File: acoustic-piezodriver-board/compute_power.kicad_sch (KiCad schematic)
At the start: 26 parts, among them J301 Conn_02x06_Odd_Even, U10 NCE6005AS, U9 LM3478MM

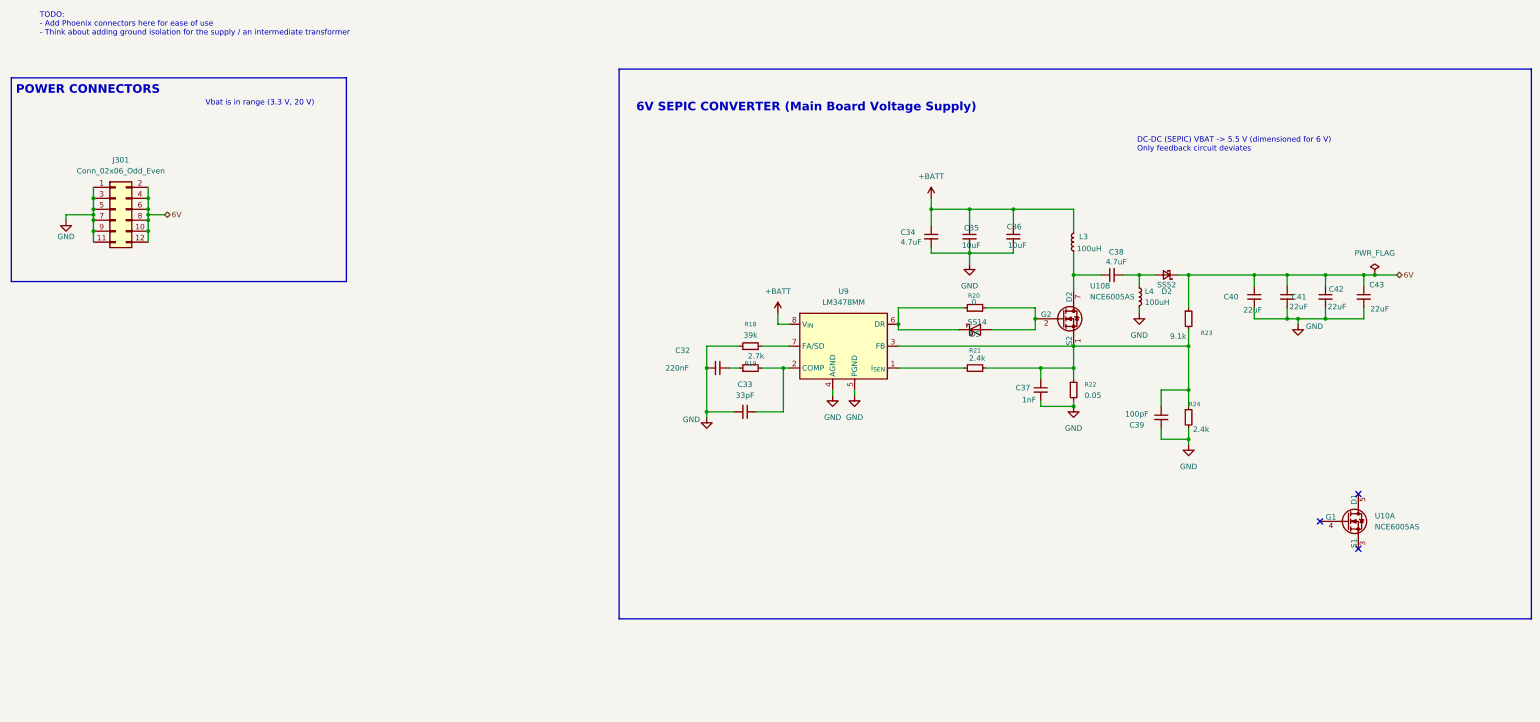
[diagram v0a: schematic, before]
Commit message: [schematic] added adc for temperature measurement, current sense resistors, [layout] component placement, connector placement
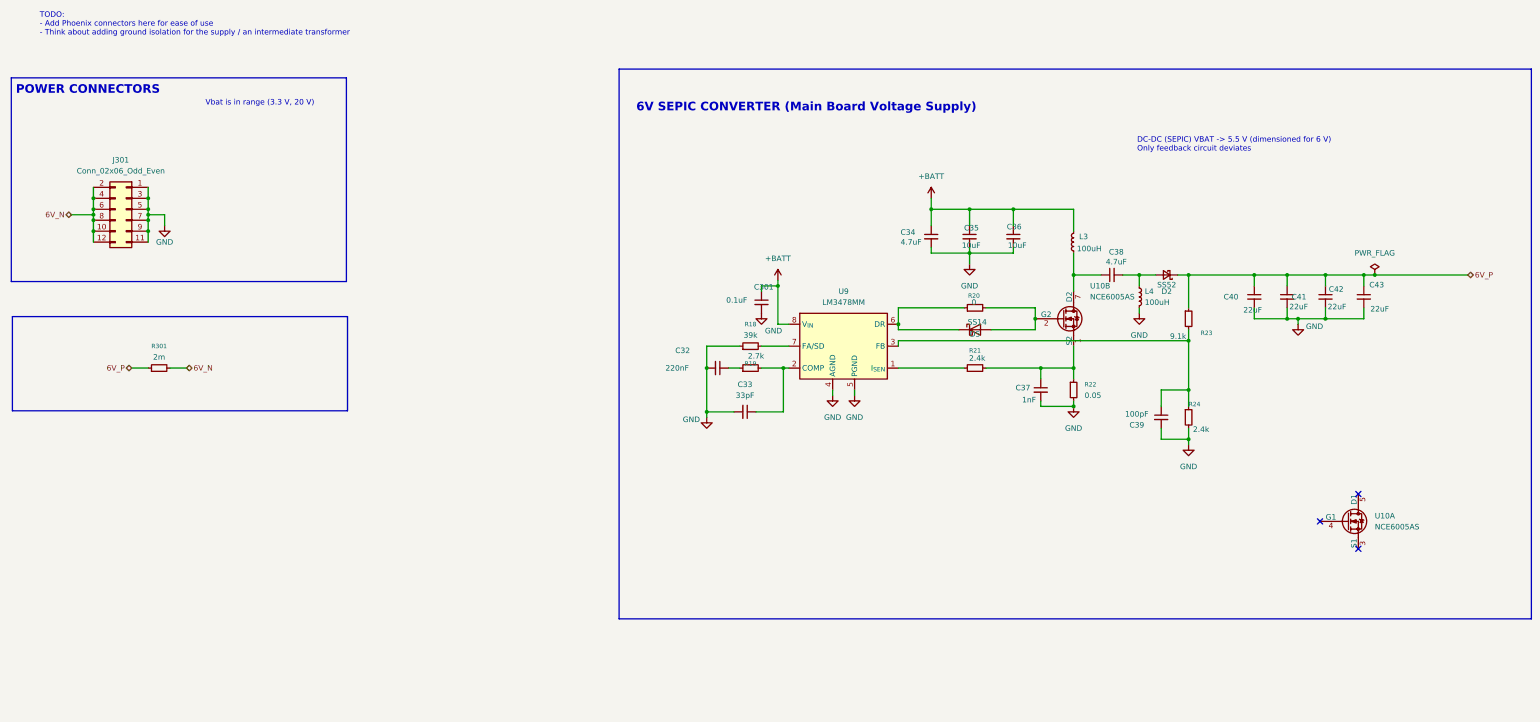
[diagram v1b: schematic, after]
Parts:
- added C301: 0.1uF, Capacitor_SMD:C_0201_0603Metric, symbol Device:C_Small
- added R301: 2m, Resistor_SMD:R_2512_6332Metric, symbol Device:R_Small
- J301: footprint Connector_PinHeader_2.54mm:PinHeader_2x06_P2.54mm_Horizontal -> Connector_PinHeader_2.54mm:PinHeader_2x06_P2.54mm_Vertical; LPN (none) -> C124388; MPN (none) -> B-2100S12P-B110
- L4: footprint (none) -> iw-inductor:PSPMAC1045H-101M-ANP
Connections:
- net +BATT: now also C301.1
- net GND: now also C301.2
- net at C39.1, R23.2, R24.1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: no longer C37.1, R21.2, R22.1, U10.1 (S2)
- net 6V renamed 6V_N
- net 6V_N: now also R301.2; no longer C40.1, C41.1, C42.1, C43.1, D2.1 (K), R23.1
- new net: C37.1, R21.2, R22.1, U10.1 (S2)
- new net 6V_P: C40.1, C41.1, C42.1, C43.1, D2.1 (K), R23.1, R301.1

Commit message: found hal-sensor, replaced with different one for lower voltage signal source impedance, reorganised schematic
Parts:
- added C302: 0.1uF, Capacitor_SMD:C_0402_1005Metric, symbol Device:C_Small
- added C303: 1nF, Capacitor_SMD:C_0402_1005Metric, symbol Device:C_Small
- added TP301: TestPoint_Probe, TestPoint:TestPoint_Pad_D1.0mm, symbol Connector:TestPoint_Probe
- added U301: ACS711xEXLT-15AB, Sensor_Current:Allegro_QFN-12-10-1EP_3x3mm_P0.5mm, symbol Sensor_Current:ACS711xEXLT-15AB
- R301: value 2m -> 1k; footprint Resistor_SMD:R_2512_6332Metric -> Resistor_SMD:R_0603_1608Metric; LPN C160590 -> C21190; MPN RLP25FEER002 -> 0603WAF1001T5E
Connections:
- net 6V_N: now also U301.2 (IP-); no longer R301.2
- net 6V_P: now also U301.1 (IP+); no longer R301.1
- net GND: now also C302.2, C303.2, U301.3 (GND), U301.5 (NC), U301.6 (NC), U301.7 (NC), U301.8 (NC)
- new net: R301.2, TP301.1, U301.4 (~{FAULT})
- new net +3V3: C302.1, R301.1, U301.10 (VCC)
- new net ADC_IFPGA: C303.1, U301.9 (VIOUT)
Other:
- note added: "- Differential -> Single-ended input - Buffering - Amplification (range 0.1 -> 2 Amps), increments of 0.01"
- note added: "I_FPGA measurement"

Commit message: added new notes + schematic component hal sensors
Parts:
- removed C302: 0.1uF, Capacitor_SMD:C_0402_1005Metric, symbol Device:C_Small
- removed C303: 1nF, Capacitor_SMD:C_0402_1005Metric, symbol Device:C_Small
- removed R301: 1k, Resistor_SMD:R_0603_1608Metric, symbol Device:R_Small
- removed TP301: TestPoint_Probe, TestPoint:TestPoint_Pad_D1.0mm, symbol Connector:TestPoint_Probe
- removed U301: ACS711xEXLT-15AB, Sensor_Current:Allegro_QFN-12-10-1EP_3x3mm_P0.5mm, symbol Sensor_Current:ACS711xEXLT-15AB
- added C304: 0.1uF, Capacitor_SMD:C_0402_1005Metric, symbol Device:C_Small
- added TP301: TestPoint_Flag, TestPoint:TestPoint_THTPad_D2.0mm_Drill1.0mm, symbol Connector:TestPoint_Flag
- added U302: TMCS1108A3UQDR, iw-power:TMCS1108A3UQDR, symbol iw-power:TMCS1108A3UQDR
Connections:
- net 6V_N: now also U302.3 (IN-), U302.4 (IN-)
- net ADC_IFPGA: now also U302.7 (VOUT)
- net GND: now also C304.2, U302.5 (GND)
- net 6V_P renamed +6V
- net +6V: now also C304.1, TP301.1, U302.1 (IN+), U302.2 (IN+), U302.8 (VS)
- no-connect marks 3 -> 4

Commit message: finished schematic, routing
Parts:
- removed L3: 100uH, symbol Device:L_Small
- removed L4: 100uH, iw-inductor:PSPMAC1045H-101M-ANP, symbol Device:L_Small
- added L301, L302: 100uH, iw-inductor:PSPMAA1050H-101M-ANP, symbol Device:L_Small
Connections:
- net +BATT: now also L301.1
- net GND: now also L302.2
- net at C38.1, U10.7 (D2), U10.8 (D2): now also L301.2
- net at C38.2, D2.2 (A): now also L302.1
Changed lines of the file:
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@@
+	)
+	(symbol
+		(lib_id "Device:L_Small")
+		(at 280.67 82.55 0)
+		(unit 1)
+		(exclude_from_sim no)
+		(in_bom yes)
+		(on_board yes)
+		(dnp no)
+		(fields_autoplaced yes)
+		(property "Reference" "L302"
+			(at 281.94 81.2799 0)
+			(effects
+				(font
+					(size 1.27 1.27)
+				)
+				(justify left)
+			)
+		)
+		(property "Value" "100uH"
+			(at 281.94 83.8199 0)
+			(effects
+				(font
+					(size 1.27 1.27)
+				)
+				(justify left)
+			)
+		)
+		(property "Footprint" "iw-inductor:PSPMAA1050H-101M-ANP"
+			(at 280.67 82.55 0)
+			(effects
+				(font
+					(size 1.27 1.27)
+				)
+				(hide yes)
+			)
+		)
+		(property "Datasheet" "https://jlcpcb.com/api/file/downloadByFileSystemAccessId/8588935627815862272"
+			(at 280.67 82.55 0)
+			(effects
+				(font
+					(size 1.27 1.27)
+				)
+				(hide yes)
+			)
+		)
+		(property "Description" "+-20%, DCR 0.25, Isat_rms=3A"
+			(at 280.67 82.55 0)
+			(effects
+				(font
+					(size 1.27 1.27)
+				)
+				(hide yes)
+			)
+		)
+		(property "LPN" "C5273830"
+			(at 280.67 82.55 0)
+			(effects
+				(font
+					(size 1.27 1.27)
+				)
+				(hide yes)
+			)
+		)
+		(property "MPN" "PSPMAA1050H-101M-ANP "
+			(at 280.67 82.55 0)
+			(effects
+				(font
+					(size 1.27 1.27)
+				)
+				(hide yes)
+			)
+		)
+		(pin "2"
+		)
+		(pin "1"
+		)
+		(instances
+			(project "acoustic-piezodriver-board"
+				(path "/94cb090f-214e-44cc-b8ed-ae50ff29d2bf/a0fbc78d-8163-4e6b-8d81-98a3dd6573cb"
+					(reference "L302")
+					(unit 1)
+				)
+			)
+		)
 	)
 	(symbol
@@
 	)
 	(symbol
-		(lib_id "Device:L_Small")
-		(at 265.43 69.85 180)
-		(unit 1)
-		(exclude_from_sim no)
-		(in_bom yes)
-		(on_board yes)
-		(dnp no)
-		(property "Reference" "L3"
-			(at 266.7 68.5799 0)
-			(effects
-				(font
-					(size 1.27 1.27)
-				)
-				(justify right)
-			)
-		)
-		(property "Value" "100uH"
-			(at 266.192 71.374 0)
-			(effects
-				(font
-					(size 1.27 1.27)
-				)
-				(justify right)
-			)
-		)
-		(property "Footprint" ""
-			(at 265.43 69.85 0)
-			(effects
-				(font
-					(size 1.27 1.27)
-				)
-				(hide yes)
-			)
-		)
-		(property "Datasheet" "https://jlcpcb.com/api/file/downloadByFileSystemAccessId/8588935627815862272"
-			(at 265.43 69.85 0)
-			(effects
-				(font
-					(size 1.27 1.27)
-				)
-				(hide yes)
-			)
-		)
-		(property "Description" "+-20%, DCR 0.25, Isat_rms=2A"
-			(at 265.43 69.85 0)
-			(effects
-				(font
-					(size 1.27 1.27)
-				)
-				(hide yes)
-			)
-		)
-		(property "LPN" "C436577"
-			(at 265.43 69.85 0)
-			(effects
-				(font
-					(size 1.27 1.27)
-				)
-				(hide yes)
-			)
-		)
-		(property "MPN" "PSPMAC1045H-101M-ANP"
-			(at 265.43 69.85 0)
-			(effects
-				(font
-					(size 1.27 1.27)
-				)
-				(hide yes)
-			)
-		)
-		(pin "2"
-		)
-		(pin "1"
-		)
-		(instances
-			(project "acoustic-piezodriver-board"
-				(path "/94cb090f-214e-44cc-b8ed-ae50ff29d2bf/a0fbc78d-8163-4e6b-8d81-98a3dd6573cb"
-					(reference "L3")
-					(unit 1)
-				)
-			)
-		)
-	)
-	(symbol
 		(lib_id "Device:D_Schottky_Small")
 		(at 287.02 77.47 180)
@@
 	)
 	(symbol
-		(lib_id "Device:L_Small")
-		(at 280.67 82.55 0)
-		(unit 1)
-		(exclude_from_sim no)
-		(in_bom yes)
-		(on_board yes)
-		(dnp no)
-		(fields_autoplaced yes)
-		(property "Reference" "L4"
-			(at 281.94 81.2799 0)
-			(effects
-				(font
-					(size 1.27 1.27)
-				)
-				(justify left)
-			)
-		)
-		(property "Value" "100uH"
-			(at 281.94 83.8199 0)
-			(effects
-				(font
-					(size 1.27 1.27)
-				)
-				(justify left)
-			)
-		)
-		(property "Footprint" "iw-inductor:PSPMAC1045H-101M-ANP"
-			(at 280.67 82.55 0)
-			(effects
-				(font
-					(size 1.27 1.27)
-				)
-				(hide yes)
-			)
-		)
-		(property "Datasheet" "https://jlcpcb.com/api/file/downloadByFileSystemAccessId/8588935627815862272"
-			(at 280.67 82.55 0)
-			(effects
-				(font
-					(size 1.27 1.27)
-				)
-				(hide yes)
-			)
-		)
-		(property "Description" "+-20%, DCR 0.25, Isat_rms=2A"
-			(at 280.67 82.55 0)
-			(effects
-				(font
-					(size 1.27 1.27)
-				)
-				(hide yes)
-			)
-		)
-		(property "LPN" "C436577"
-			(at 280.67 82.55 0)
-			(effects
-				(font
-					(size 1.27 1.27)
-				)
-				(hide yes)
-			)
-		)
-		(property "MPN" "PSPMAC1045H-101M-ANP"
-			(at 280.67 82.55 0)
-			(effects
-				(font
-					(size 1.27 1.27)
-				)
-				(hide yes)
-			)
-		)
-		(pin "2"
-		)
-		(pin "1"
-		)
-		(instances
-			(project "acoustic-piezodriver-board"
-				(path "/94cb090f-214e-44cc-b8ed-ae50ff29d2bf/a0fbc78d-8163-4e6b-8d81-98a3dd6573cb"
-					(reference "L4")
-					(unit 1)
-				)
-			)
-		)
-	)
-	(symbol
 		(lib_id "custom_mosfet:NCE6005AS")
 		(at 265.43 87.63 0)
@@
 	)
 	(symbol
+		(lib_id "Device:L_Small")
+		(at 265.43 69.85 0)
+		(unit 1)
+		(exclude_from_sim no)
+		(in_bom yes)
+		(on_board yes)
+		(dnp no)
+		(fields_autoplaced yes)
+		(property "Reference" "L301"
+			(at 266.7 68.5799 0)
+			(effects
+				(font
+					(size 1.27 1.27)
+				)
+				(justify left)
+			)
+		)
+		(property "Value" "100uH"
+			(at 266.7 71.1199 0)
+			(effects
+				(font
+					(size 1.27 1.27)
+				)
+				(justify left)
+			)
+		)
+		(property "Footprint" "iw-inductor:PSPMAA1050H-101M-ANP"
+			(at 265.43 69.85 0)
+			(effects
+				(font
+					(size 1.27 1.27)
+				)
+				(hide yes)
+			)
+		)
+		(property "Datasheet" "https://jlcpcb.com/api/file/downloadByFileSystemAccessId/8588935627815862272"
+			(at 265.43 69.85 0)
+			(effects
+				(font
+					(size 1.27 1.27)
+				)
+				(hide yes)
+			)
+		)
+		(property "Description" "+-20%, DCR 0.25, Isat_rms=3A"
+			(at 265.43 69.85 0)
+			(effects
+				(font
+					(size 1.27 1.27)
+				)
+				(hide yes)
+			)
+		)
+		(property "LPN" "C5273830"
+			(at 265.43 69.85 0)
+			(effects
+				(font
+					(size 1.27 1.27)
+				)
+				(hide yes)
+			)
+		)
+		(property "MPN" "PSPMAA1050H-101M-ANP "
+			(at 265.43 69.85 0)
+			(effects
+				(font
+					(size 1.27 1.27)
+				)
+				(hide yes)
+			)
+		)
+		(pin "2"
+		)
+		(pin "1"
+		)
+		(instances
+			(project "acoustic-piezodriver-board"
+				(path "/94cb090f-214e-44cc-b8ed-ae50ff29d2bf/a0fbc78d-8163-4e6b-8d81-98a3dd6573cb"
+					(reference "L301")
+					(unit 1)
+				)
+			)
+		)
+	)
+	(symbol
 		(lib_id "power:GND")
 		(at 317.5 88.9 0)
@@
 		(on_board yes)
 		(dnp no)
-		(fields_autoplaced yes)
 		(property "Reference" "#PWR044"
 			(at 280.67 92.71 0)
@@
 		)
 		(property "Value" "GND"
-			(at 280.67 91.44 0)
-			(effects
-				(font
+			(at 283.972 87.122 0)
+			(effects
+				(font

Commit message: replaced dual 10uH inductors with single 22uH higher VDC resistant one, started laying out 40 V boost
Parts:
- removed TP301: TestPoint_Flag, TestPoint:TestPoint_THTPad_D2.0mm_Drill1.0mm, symbol Connector:TestPoint_Flag
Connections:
- net GND: now also U302.6 (NC)
- no-connect marks 4 -> 3
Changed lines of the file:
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@@
 	)
 	(junction
+		(at 57.15 146.05)
+		(diameter 0)
+		(color 0 0 0 0)
+	)
+	(junction
 		(at 292.1 104.14)
 		(diameter 0)
@@
 	)
 	(junction
-		(at 345.44 77.47)
-		(diameter 0)
-		(color 0 0 0 0)
-	)
-	(junction
 		(at 256.54 87.63)
 		(diameter 0)
@@
 		(at 331.47 140.97)
 	)
-	(no_connect
-		(at 58.42 140.97)
-	)
 	(wire
 		(pts
@@
 	(wire
 		(pts
-			(xy 38.1 135.89) (xy 58.42 135.89)
+			(xy 36.83 140.97) (xy 45.72 140.97)
 		)
 		(stroke
@@
 	(wire
 		(pts
+			(xy 45.72 140.97) (xy 45.72 135.89)
+		)
+		(stroke
+			(width 0)
+			(type default)
+		)
+	)
+	(wire
+		(pts
 			(xy 292.1 113.03) (xy 292.1 115.57)
 		)
@@
 	(wire
 		(pts
+			(xy 45.72 135.89) (xy 58.42 135.89)
+		)
+		(stroke
+			(width 0)
+			(type default)
+		)
+	)
+	(wire
+		(pts
 			(xy 224.79 90.17) (xy 224.79 88.9)
 		)
@@
 	(wire
 		(pts
-			(xy 241.3 62.23) (xy 251.46 62.23)
+			(xy 57.15 146.05) (xy 58.42 146.05)
 		)
 		(stroke
@@
 	(wire
 		(pts
-			(xy 345.44 77.47) (xy 351.79 77.47)
+			(xy 241.3 62.23) (xy 251.46 62.23)
 		)
 		(stroke
@@
 	(wire
 		(pts
-			(xy 345.44 69.85) (xy 345.44 77.47)
+			(xy 332.74 85.09) (xy 332.74 87.63)
 		)
 		(stroke
@@
 	(wire
 		(pts
-			(xy 332.74 85.09) (xy 332.74 87.63)
+			(xy 307.34 87.63) (xy 314.96 87.63)
 		)
 		(stroke
@@
 	(wire
 		(pts
-			(xy 307.34 87.63) (xy 314.96 87.63)
+			(xy 57.15 140.97) (xy 57.15 146.05)
 		)
 		(stroke
@@
 	(wire
 		(pts
+			(xy 57.15 140.97) (xy 58.42 140.97)
+		)
+		(stroke
+			(width 0)
+			(type default)
+		)
+	)
+	(wire
+		(pts
 			(xy 245.11 99.06) (xy 257.81 99.06)
 		)
@@
 	(wire
 		(pts
-			(xy 58.42 149.86) (xy 58.42 146.05)
+			(xy 57.15 149.86) (xy 57.15 146.05)
 		)
 		(stroke
@@
 	(wire
 		(pts
-			(xy 335.28 77.47) (xy 345.44 77.47)
+			(xy 335.28 77.47) (xy 351.79 77.47)
 		)
 		(stroke
@@
 	(hierarchical_label "ADC_IFPGA"
 		(shape output)
-		(at 38.1 135.89 180)
+		(at 36.83 140.97 180)
 		(effects
 			(font
@@
 	(symbol
 		(lib_id "power:GND")
-		(at 58.42 149.86 0)
+		(at 57.15 149.86 0)
 		(unit 1)
 		(exclude_from_sim no)
@@
 		(fields_autoplaced yes)
 		(property "Reference" "#PWR0307"
-			(at 58.42 156.21 0)
+			(at 57.15 156.21 0)
 			(effects
 				(font
@@
 		)
 		(property "Value" "GND"
-			(at 58.42 154.94 0)
+			(at 57.15 154.94 0)
 			(effects
 				(font
@@
 		)
 		(property "Footprint" ""
-			(at 58.42 149.86 0)
+			(at 57.15 149.86 0)
 			(effects
 				(font
@@
 		)
 		(property "Datasheet" ""
-			(at 58.42 149.86 0)
+			(at 57.15 149.86 0)
 			(effects
 				(font
@@
 		)
 		(property "Description" "Power symbol creates a global label with name \"GND\" , ground"
-			(at 58.42 149.86 0)
+			(at 57.15 149.86 0)
 			(effects
 				(font
@@
 					(unit 1)
 				)
-			)
-		)
-	)
-	(symbol
-		(lib_id "Connector:TestPoint_Flag")
-		(at 345.44 69.85 0)
-		(mirror y)
-		(unit 1)
-		(exclude_from_sim no)
-		(in_bom yes)
-		(on_board yes)
-		(dnp no)
-		(property "Reference" "TP301"
-			(at 339.344 64.77 0)
-			(effects
-				(font
-					(size 1.27 1.27)
-				)
-				(justify left)
-			)
-		)
-		(property "Value" "TestPoint_Flag"
-			(at 338.328 67.056 0)
-			(effects
-				(font
-					(size 1.27 1.27)
-				)
-				(justify left)
-			)
-		)
-		(property "Footprint" "TestPoint:TestPoint_THTPad_D2.0mm_Drill1.0mm"
-			(at 340.36 69.85 0)
-			(effects
-				(font
-					(size 1.27 1.27)
-				)
-				(hide yes)
-			)
-		)
-		(property "Datasheet" "~"
-			(at 340.36 69.85 0)
-			(effects
-				(font
-					(size 1.27 1.27)
-				)
-				(hide yes)
-			)
-		)
-		(property "Description" "test point (alternative flag-style design)"
-			(at 345.44 69.85 0)
-			(effects
-				(font
-					(size 1.27 1.27)
-				)
-				(hide yes)
-			)
-		)
-		(pin "1"
-		)
-		(instances
-			(project "acoustic-piezodriver-board"
-				(path "/94cb090f-214e-44cc-b8ed-ae50ff29d2bf/a0fbc78d-8163-4e6b-8d81-98a3dd6573cb"
-					(reference "TP301")
-					(unit 1)
-				)

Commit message: placed inverter and 40 V boost (next) place 10 V SEPIC driver
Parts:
- U9: LPN (none) -> C404045; MPN (none) -> LM3478MMX/NOPB
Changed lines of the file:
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@@
+			)
+		)
+		(property "LPN" "C404045"
+			(at 212.09 93.98 0)
+			(effects
+				(font
+					(size 1.27 1.27)
+				)
+				(hide yes)
+			)
+		)
+		(property "MPN" "LM3478MMX/NOPB "
+			(at 212.09 93.98 0)
+			(effects
+				(font
+					(size 1.27 1.27)
+				)
+				(hide yes)
 			)
 		)
